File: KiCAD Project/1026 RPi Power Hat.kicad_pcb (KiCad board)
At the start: 4 copper layers, 85 x 56.5 mm, 132 parts, among them J1 S2B-XH-A-1, J2 B2B-XH-A(LF)(SN), J3 ESW-120-33-G-D, J4 USB1030-GF-P-B-B, J5 USB1035-GF-P-0-B-B, J6 USB1035-GF-P-0-B-B, M1 CFM-2510B-070-140, P1 DW_PCB_Logo, P2 Raspberry Pi HAT+ Designator, Q1 BUK6D120-60PX, U1 LM64440APPQRYFRQ1, U10 USBLC6-2P6, U11 USBLC6-2P6, U12 USBLC6-2P6, U2 TLV75511PDQNR, U3 TLV75533PDQNR, U4 TUSB4041IPAPR, U5 TPS2561DRCR, U6 TPS2561DRCR, U7 CAT24C32HU4I-GT3, U8 USBLC6-2P6, U9 USBLC6-2P6, Y1 ECS-2520MV-240-BL-TR

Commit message: New BOM for new Parts
Add ESW-120-34-G-D and remove ESW-120-33-G-D.  Update BOM and iBOM.
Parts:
- J3: value ESW-120-33-G-D -> ESW-120-34-G-D; footprint 1026-3D:[J] Samtec Elevated Socket Strip ESW-120-33-G-D -> 1026-3D:[J] Samtec Elevated Socket Strip ESW-120-34-G-D
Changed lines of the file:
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@@
 			)
 		)
-		(property "Datasheet" ""
+		(property "Datasheet" "~"
 			(at 0 0 0)
 			(layer "F.Fab")
@@
 			)
 		)
-		(property "Datasheet" ""
+		(property "Datasheet" "~"
 			(at 0 0 0)
 			(layer "F.Fab")
@@
 			)
 		)
-		(property "Datasheet" ""
+		(property "Datasheet" "~"
 			(at 0 0 0)
 			(layer "F.Fab")
@@
 			)
 		)
-		(property "Datasheet" ""
+		(property "Datasheet" "~"
 			(at 0 0 0)
 			(unlocked yes)
@@
 			)
 		)
-		(property "Datasheet" ""
+		(property "Datasheet" "~"
 			(at 0 0 0)
 			(layer "F.Fab")
@@
 			)
 		)
-		(property "Datasheet" ""
+		(property "Datasheet" "~"
 			(at 0 0 0)
 			(unlocked yes)
@@
 			)
 		)
-		(property "Datasheet" ""
+		(property "Datasheet" "~"
 			(at 0 0 0)
 			(unlocked yes)
@@
 		(embedded_fonts no)
 	)
-	(footprint "1026-3D:[J] Samtec Elevated Socket Strip ESW-120-33-G-D"
+	(footprint "1026-3D:[J] Samtec Elevated Socket Strip ESW-120-34-G-D"
 		(layer "B.Cu")
 		(at 132.5 97.5 180)
-		(descr "Elevated Socket Strip 0.1in 20x2 16.13mmH Gold")
-		(tags "Elevated Socket Strip 0.1in 20x2 16.13mmH Gold")
+		(descr "Elevated Socket Strip 0.28in 20x2 16.13mmH Gold")
+		(tags "Elevated Socket Strip 0.28in 20x2 16.13mmH Gold")
 		(property "Reference" "J3"
-			(at 24 -3.7 180)
+			(at 24.089728 -3.475245 0)
 			(layer "B.SilkS")
 			(effects
 				(font
-					(size 1.27 1.27)
-					(thickness 0.254)
-					(bold yes)
+					(size 1 1)
+					(thickness 0.15)
 				)
 				(justify mirror)
 			)
 		)
-		(property "Value" "ESW-120-33-G-D"
-			(at -13.32 -4.34 180)
+		(property "Value" "ESW-120-34-G-D"
+			(at -13.32 -4.34 0)
 			(layer "B.Fab")
 			(effects
@@
 		)
 		(property "Datasheet" "https://www.mouser.com/datasheet/2/527/esw_th-2854089.pdf"
-			(at 0 0 180)
+			(at 0 0 0)
 			(layer "B.Fab")
 			(hide yes)
@@
 			)
 		)
-		(property "Description" "Elevated Socket Strip 0.1in 20x2 16.13mmH Gold"
-			(at 0 0 180)
+		(property "Description" "Elevated Socket Strip 0.28in 20x2 16.13mmH Gold"
+			(at 0 0 0)
 			(layer "B.Fab")
 			(hide yes)
@@
 			)
 		)
-		(property "Height" "16.13"
+		(property "Manufacturer_Name" "Samtec"
 			(at 0 0 0)
-			(unlocked yes)
 			(layer "B.Fab")
 			(hide yes)
@@
 				(font
 					(size 1 1)
-					(thickness 0.15)
+					(thickness 0.1)
 				)
 				(justify mirror)
 			)
 		)
-		(property "Manufacturer_Name" "Samtec"
+		(property "Height" "16.13"
 			(at 0 0 0)
-			(unlocked yes)
 			(layer "B.Fab")
 			(hide yes)
@@
 				(font
 					(size 1 1)
-					(thickness 0.15)
+					(thickness 0.1)
 				)
 				(justify mirror)
 			)
 		)
-		(property "Manufacturer_Part_Number" "ESW-120-33-G-D"
+		(property "Manufacturer_Part_Number" "ESW-120-34-G-D"
 			(at 0 0 0)
-			(unlocked yes)
 			(layer "B.Fab")
 			(hide yes)
@@
 				(font
 					(size 1 1)
-					(thickness 0.15)
+					(thickness 0.1)
 				)
 				(justify mirror)
 			)
 		)
-		(property "Mouser Part Number" "200-ESW12033GD"
+		(property "Mouser Part Number" "200-ESW12034GD"
 			(at 0 0 0)
-			(unlocked yes)
 			(layer "B.Fab")
 			(hide yes)
@@
 				(font
 					(size 1 1)
-					(thickness 0.15)
+					(thickness 0.1)
 				)
 				(justify mirror)
 			)
 		)
-		(property "Mouser Price/Stock" "https://www.mouser.com/ProductDetail/Samtec/ESW-120-33-G-D?qs=0lQeLiL1qybGjRGIrteP4Q%3D%3D"
+		(property "Mouser Price/Stock" "https://www.mouser.com/ProductDetail/Samtec/ESW-120-34-G-D?qs=0lQeLiL1qyZhSkNUS%2FXSIA%3D%3D"
 			(at 0 0 0)
-			(unlocked yes)
 			(layer "B.Fab")
 			(hide yes)
@@
 				(font
 					(size 1 1)
-					(thickness 0.15)
+					(thickness 0.1)
 				)
 				(justify mirror)
 			)
 		)
-		(property "Spec" "20x2 0.1\" Header"
+		(property "Spec" "20x2 0.28\" Header"
 			(at 0 0 0)
-			(unlocked yes)
 			(layer "B.Fab")
 			(hide yes)
@@
 				(font
 					(size 1 1)
-					(thickness 0.15)
+					(thickness 0.1)
 				)
 				(justify mirror)

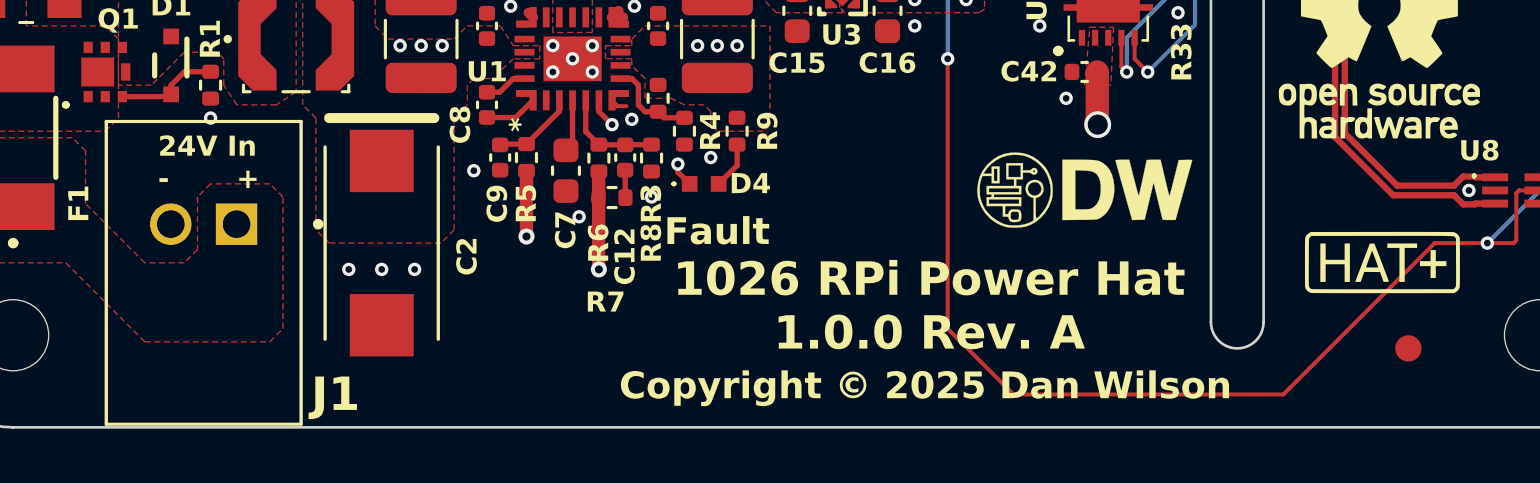
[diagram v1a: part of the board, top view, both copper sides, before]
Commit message: Prep for PCBway
Verified all parts reference local libraries, update font for PCB board title to Noto Sans font, add Noto Sans fonts to project folder, update 3D image for documentation, update documentation for links to both Oshpark and PCBway .zip files.
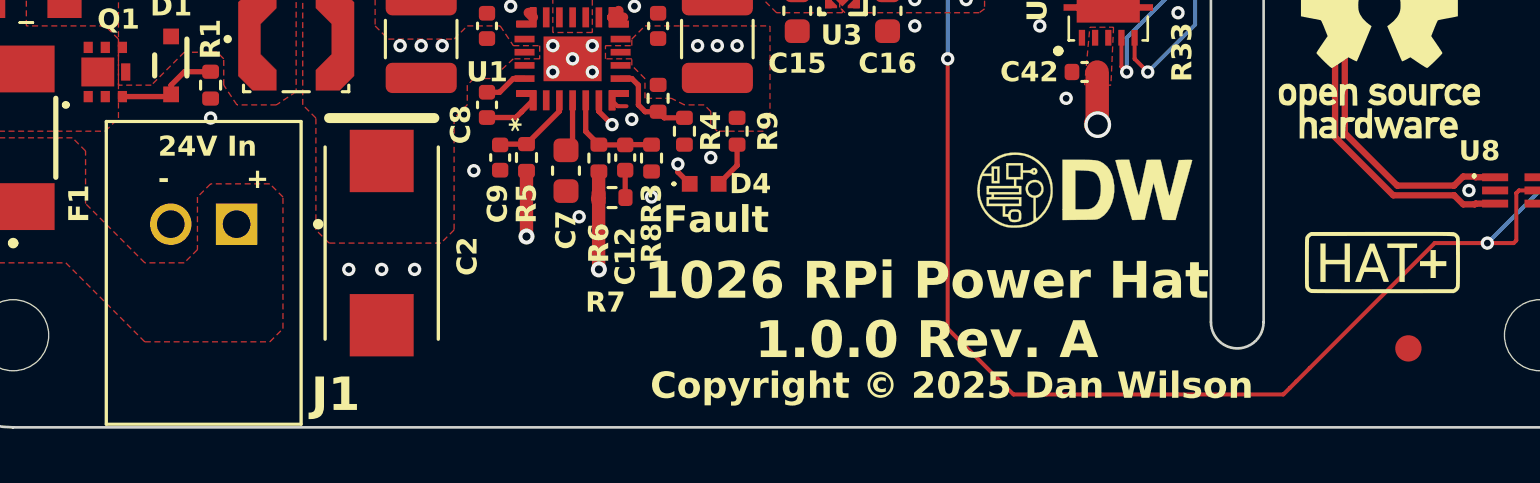
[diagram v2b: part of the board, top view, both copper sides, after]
